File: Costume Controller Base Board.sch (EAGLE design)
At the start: 46 parts, among them J1 USB MICRO, U1 ATMEGA32U4-XUMU, U4 MPU-6050-1, U5 TPS61200, Y1 16MHz KX-7

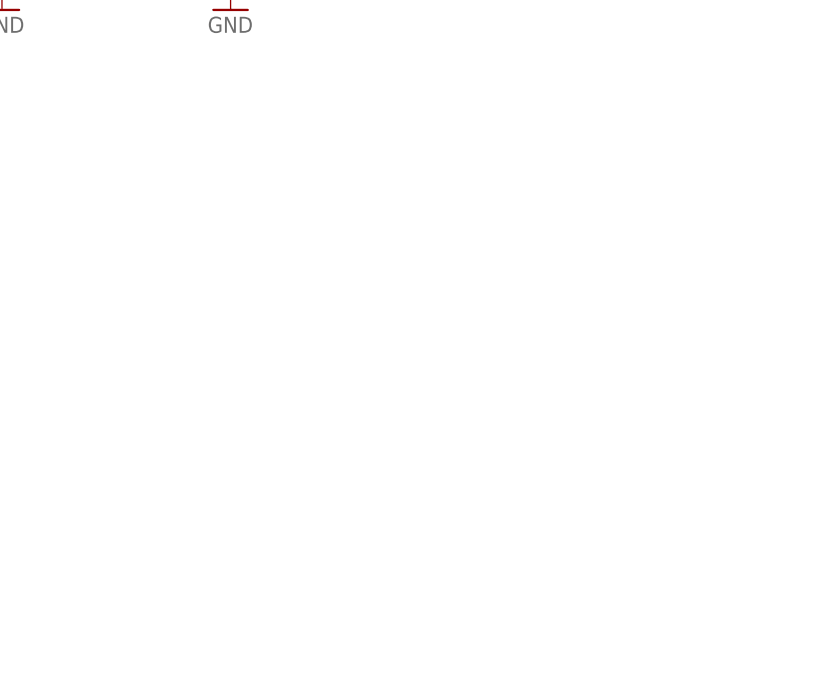
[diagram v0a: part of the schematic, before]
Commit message: Added 3.3v regulator
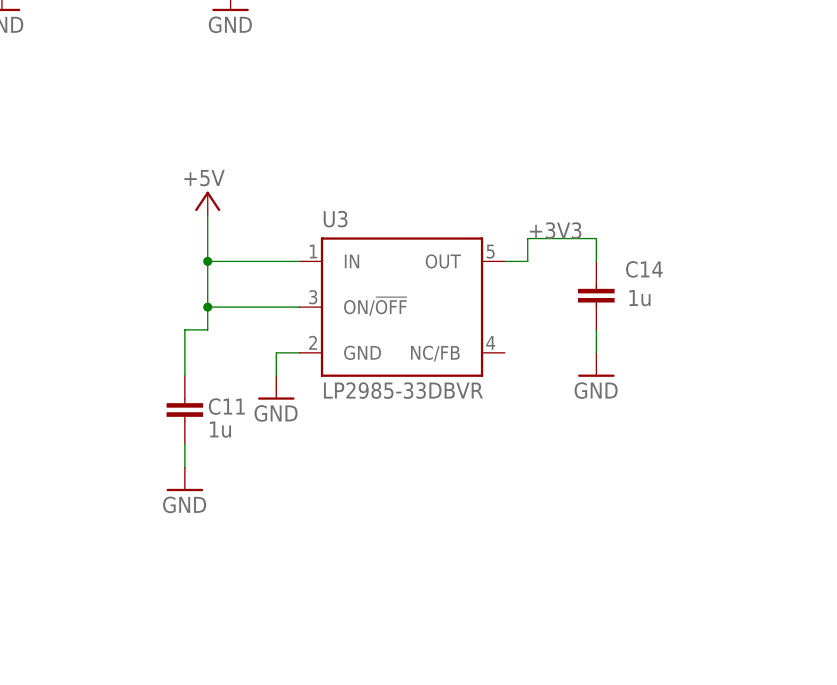
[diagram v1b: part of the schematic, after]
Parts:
- added C11, C14: 1u, SmartPrj:C-EUC0603
- added U3: LP2985-33DBVR, SmartPrj:LP2985-XXDBVR33
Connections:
- new net +3V3: C14.2, U3.OUT
- net +5V: now also C11.2, U3.IN, U3.ON/!OFF
- net GND: now also C11.1, C14.1, U3.GND
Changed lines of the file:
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@@
 <part name="L3" library="SparkFun" deviceset="INDUCTOR" device="." value="4.7uH, 1.2A"/>
 <part name="U$1" library="MyPOW" deviceset="+5V" device=""/>
+<part name="C11" library="SmartPrj" deviceset="C-EU" device="C0603" value="1u"/>
+<part name="GND7" library="supply1" deviceset="GND" device=""/>
+<part name="C14" library="SmartPrj" deviceset="C-EU" device="C0603" value="1u"/>
+<part name="P+10" library="supply1" deviceset="+5V" device=""/>
+<part name="GND21" library="supply1" deviceset="GND" device=""/>
+<part name="U3" library="SmartPrj" deviceset="LP2985-XXDBVR" device="" technology="33" value="LP2985-33DBVR"/>
+<part name="GND13" library="supply1" deviceset="GND" device=""/>
 </parts>
 <sheets>
@@
 </instance>
 <instance part="U$1" gate="G$1" x="-1084.58" y="325.12"/>
+<instance part="C11" gate="G$1" x="-1094.74" y="152.4" smashed="yes" rot="MR180">
+<attribute name="NAME" x="-1092.2" y="154.94" size="1.778" layer="95" rot="MR180"/>
+<attribute name="VALUE" x="-1092.2" y="152.4" size="1.778" layer="96" rot="MR180"/>
+</instance>
+<instance part="GND7" gate="1" x="-1094.74" y="144.78"/>
+<instance part="C14" gate="G$1" x="-1049.02" y="165.1" smashed="yes" rot="R180">
+<attribute name="NAME" x="-1045.845" y="168.402" size="1.778" layer="95"/>
+<attribute name="VALUE" x="-1045.591" y="165.227" size="1.778" layer="96"/>
+</instance>
+<instance part="P+10" gate="1" x="-1092.2" y="177.8" smashed="yes">
+<attribute name="VALUE" x="-1090.295" y="180.34" size="1.778" layer="96" rot="R180"/>
+</instance>
+<instance part="GND21" gate="1" x="-1049.02" y="157.48"/>
+<instance part="U3" gate="G$1" x="-1071.88" y="165.1" smashed="yes">
+<attribute name="NAME" x="-1079.5" y="173.99" size="1.778" layer="95" font="vector"/>
+<attribute name="VALUE" x="-1079.5" y="154.94" size="1.778" layer="96" font="vector"/>
+</instance>
+<instance part="GND13" gate="1" x="-1084.58" y="154.94"/>
 </instances>
 <busses>
@@
 <junction x="-1092.2" y="320.04"/>
 <pinref part="U$1" gate="G$1" pin="+5V"/>
+</segment>
+<segment>
+<wire x1="-1082.04" y1="165.1" x2="-1092.2" y2="165.1" width="0.1524" layer="91"/>
+<wire x1="-1092.2" y1="165.1" x2="-1092.2" y2="170.18" width="0.1524" layer="91"/>
+<wire x1="-1092.2" y1="170.18" x2="-1092.2" y2="175.26" width="0.1524" layer="91"/>
+<wire x1="-1082.04" y1="170.18" x2="-1092.2" y2="170.18" width="0.1524" layer="91"/>
+<wire x1="-1094.74" y1="162.56" x2="-1092.2" y2="162.56" width="0.1524" layer="91"/>
+<wire x1="-1092.2" y1="162.56" x2="-1092.2" y2="165.1" width="0.1524" layer="91"/>
+<wire x1="-1094.74" y1="157.48" x2="-1094.74" y2="162.56" width="0.1524" layer="91"/>
+<junction x="-1092.2" y="170.18"/>
+<junction x="-1092.2" y="165.1"/>
+<pinref part="P+10" gate="1" pin="+5V"/>
+<pinref part="U3" gate="G$1" pin="ON/!OFF"/>
+<pinref part="U3" gate="G$1" pin="IN"/>
+<pinref part="C11" gate="G$1" pin="2"/>
 </segment>
 </net>
@@
 <junction x="-1125.22" y="289.56"/>
 </segment>
+<segment>
+<wire x1="-1094.74" y1="149.86" x2="-1094.74" y2="147.32" width="0.1524" layer="91"/>
+<pinref part="C11" gate="G$1" pin="1"/>
+<pinref part="GND7" gate="1" pin="GND"/>
+</segment>
+<segment>
+<wire x1="-1049.02" y1="160.02" x2="-1049.02" y2="162.56" width="0.1524" layer="91"/>
+<pinref part="C14" gate="G$1" pin="1"/>
+<pinref part="GND21" gate="1" pin="GND"/>
+</segment>
+<segment>
+<wire x1="-1082.04" y1="160.02" x2="-1084.58" y2="160.02" width="0.1524" layer="91"/>
+<wire x1="-1084.58" y1="160.02" x2="-1084.58" y2="157.48" width="0.1524" layer="91"/>
+<pinref part="U3" gate="G$1" pin="GND"/>
+<pinref part="GND13" gate="1" pin="GND"/>
+</segment>
 </net>
 <net name="AREF" class="4">
@@
 </segment>
 </net>
+<net name="+3V3" class="0">
+<segment>
+<wire x1="-1049.02" y1="172.72" x2="-1049.02" y2="170.18" width="0.1524" layer="91"/>
+<wire x1="-1056.64" y1="172.72" x2="-1049.02" y2="172.72" width="0.1524" layer="91"/>
+<wire x1="-1059.18" y1="170.18" x2="-1056.64" y2="170.18" width="0.1524" layer="91"/>
+<wire x1="-1056.64" y1="170.18" x2="-1056.64" y2="172.72" width="0.1524" layer="91"/>
+<label x="-1056.64" y="172.72" size="1.778" layer="95"/>
+<pinref part="C14" gate="G$1" pin="2"/>
+<pinref part="U3" gate="G$1" pin="OUT"/>
+</segment>
+</net>

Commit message: Some joining of grounds and such, need to review nets and busses, eliminated stray resistors, will replace resistor nets with discrete resistors -- www
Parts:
- removed JP6: M10", SparkFun:M10"
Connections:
- removed net N$11: J1.SH1, J1.SH2, J1.SH3, J1.SH4, J1.SH5, J1.SH6, L2.2
- net AUX_SCL: no longer JP6.2
- net AUX_SDA: no longer JP6.1
- net CLKIN: no longer JP6.3
- net FSYNC: no longer JP6.7
- net GND: now also J1.SH1, J1.SH2, J1.SH3, J1.SH4, J1.SH5, J1.SH6, L2.2; no longer JP6.9
- net INT: no longer JP6.8
- net SCL: no longer JP6.6
- net SDA: no longer JP6.5
- net VCC: no longer JP6.10
- net VIO: no longer JP6.4
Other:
- note removed: "1. 3.3v I/O for MPU, or run MCU at 3.3v."
- note removed: "NOT USED"

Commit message: modified nets, removed extraneous components
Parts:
- removed C1, C2, C6: 100n, SmartPrj:C-EUC0603
- removed C5: 1uF, SmartPrj:C-EUC0603
- removed D2: CD1206-S01575, diode:DIODE-MINIMELF
- removed F1: MF-MSMF050-2 500mA, rcl:L-EUL1812
- removed L1, L2: MH2029-300Y, wuerth-elektronik:WE-CBF_0805
- removed RN1: 10K, resistor-dil:4R-NCAY16
- removed RN3: 22R, resistor-dil:4R-NCAY16
- removed SJ1: (no value), SparkFun:SOLDERJUMPER_2WAYPASTE2&3
- removed SJ2, SJ3: SOLDERJUMPERTRACE, SparkFun:SOLDERJUMPERTRACE
- removed Z1, Z2: CG0603MLC-05E, varistor:VARISTORCN0603
- C19: device CH_passive:CAP0805 -> resistor:C-EUC0603
- R2, R3: value NM -> 22; device SmartPrj:R-EU_R0402 -> resistor:R-EU_R0603
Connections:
- removed net A0: U1.(ADC7/TDI)PF7
- removed net A1: U1.(ADC6/TDO)PF6
- removed net A2: U1.(ADC5/TMS)PF5
- removed net A3: U1.(ADC4/TCK)PF4
- removed net A4: U1.(ADC1)PF1
- removed net A5: U1.(ADC0)PF0
- removed net ADO: SJ1.2, U4.AD0
- removed net AGND: C6.1, R2.1, U1.GND3
- removed net AREF: C6.2, U1.AREF
- removed net AVCC: C5.1, L1.2, U1.AVCC, U1.AVCC1
- removed net CLKIN: SJ2.2, U4.CLKIN
- removed net D0/RX: U1.(RXD1/AIN1/INT2)PD2
- removed net D1/TX: U1.(TXD1/INT3)PD3
- removed net D2/SDA: U1.(SDA/INT1)PD1
- removed net D3/SCL: U1.(OC0B/SCL/INT0)PD0
- removed net D4: U1.(ICP1/ADC8)PD4
- removed net D5*: U1.(OC3A/#0C4A)PC6
- removed net D6*: U1.(T0/OC4D/ADC10)PD7
- removed net D7: U1.(INT6/AIN0)PE6
- removed net FSYNC: SJ3.2, U4.FSYNC
- removed net HWB: U1.(#HWB)PE2
- removed net IO10*: U1.(PCINT6/OC1B/OC4B/ADC13)PB6
- removed net IO11*: U1.(PCINT7/OC0A/OC1C/#RTS)PB7
- removed net IO12: U1.(T1/#OC4D/ADC9)PD6
- removed net IO13*: U1.(ICP3/CLK0/OC4A)PC7
- removed net IO8: U1.(ADC11/PCINT4)PB4
- removed net IO9*: U1.(PCINT5/OC1A/#OC4B/ADC12)PB5
- removed net RESET: D2.A, ICSP.5, RN1D.1, U1.RESET
- removed net RXLED: U1.(SS/PCINT0)PB0
- removed net TXLED: U1.(XCK1/#CTS)PD5
- removed net VCC: C17.1, R4.2, R5.2, SJ1.1, U4.VDD
- removed net XUSB: F1.2, J1.VBUS
- net +3V3: now also C17.1, R4.2, R5.2, U4.VDD
- net +5V: now also ICSP.5, U1.AVCC, U1.AVCC1; no longer C1.1, C2.1, D2.C, L1.1, RN1D.2
- net D+: now also R3.1; no longer RN3A.2, Z1.1
- net D-: now also R2.1; no longer RN3D.2, Z2.1
- net GND: now also U4.AD0, U4.CLKIN, U4.FSYNC; no longer C1.2, C2.2, C5.2, L2.2, R2.2, R3.1, SJ1.3, SJ2.1, SJ3.1, Z1.2, Z2.2
- net RD+: now also R3.2; no longer RN3A.1
- net RD-: now also R2.2; no longer RN3D.1
- net SCL: now also U1.(OC0B/SCL/INT0)PD0
- net SDA: now also U1.(SDA/INT1)PD1
- net UGND: no longer L2.1, R3.2
- net VUSB: now also J1.VBUS; no longer F1.1
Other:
- note added: "1. Level shift for MPU logic"
- note removed: "*"
- note removed: "**"
- note removed: "***"
- note removed: "I2C Address Selection*"
- moved on the sheet: C19, R2, R3

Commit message: added TI level translator
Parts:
- added C1: 0.1uF, SparkFun:CAP0603-CAP
- added U2: PCA9306DCUT, Texas Instruments_By_element14_Batch_1:PCA9306DCUT
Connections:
- removed net SCL: R4.1, U1.(OC0B/SCL/INT0)PD0, U4.SCL
- removed net SDA: R5.1, U1.(SDA/INT1)PD1, U4.SDA
- new net SCL2: U1.(OC0B/SCL/INT0)PD0
- new net SDA1: U4.SDA
- new net SDA2: U1.(SDA/INT1)PD1
- net +3V3: now also C1.1
- net GND: now also C1.2
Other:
- note added: "Level-shifter"
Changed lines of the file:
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@@
 <part name="R2" library="resistor" deviceset="R-EU_" device="R0603" value="22"/>
 <part name="R3" library="resistor" deviceset="R-EU_" device="R0603" value="22"/>
+<part name="U2" library="Texas Instruments_By_element14_Batch_1" deviceset="PCA9306DCUT" device=""/>
+<part name="C1" library="SparkFun" deviceset="CAP" device="0603-CAP" value="0.1uF"/>
+<part name="GND2" library="SparkFun" deviceset="GND" device=""/>
+<part name="+3V2" library="supply1" deviceset="+3V3" device=""/>
 </parts>
 <sheets>
@@
 <text x="-1231.9" y="172.72" size="1.778" layer="97">To-Do</text>
 <text x="-1231.9" y="167.64" size="1.778" layer="97">1. Level shift for MPU logic</text>
+<text x="-1013.46" y="256.54" size="1.778" layer="97">Level-shifter</text>
 </plain>
 <instances>
@@
 <instance part="R2" gate="G$1" x="-883.92" y="182.88"/>
 <instance part="R3" gate="G$1" x="-876.3" y="177.8"/>
+<instance part="U2" gate="A" x="-1021.08" y="243.84"/>
+<instance part="C1" gate="G$1" x="-1069.34" y="259.08"/>
+<instance part="GND2" gate="1" x="-1069.34" y="246.38"/>
+<instance part="+3V2" gate="G$1" x="-1069.34" y="271.78"/>
 </instances>
 <busses>
@@
 <pinref part="GND6" gate="1" pin="GND"/>
 </segment>
+<segment>
+<pinref part="GND2" gate="1" pin="GND"/>
+<pinref part="C1" gate="G$1" pin="2"/>
+<wire x1="-1069.34" y1="248.92" x2="-1069.34" y2="256.54" width="0.1524" layer="91"/>
+</segment>
 </net>
 <net name="VIN" class="1">
@@
 </segment>
 </net>
-<net name="SCL" class="0">
-<segment>
-<wire x1="-1104.9" y1="231.14" x2="-1104.9" y2="220.98" width="0.1524" layer="91"/>
-<wire x1="-1104.9" y1="220.98" x2="-1125.22" y2="220.98" width="0.1524" layer="91"/>
-<label x="-1122.68" y="220.98" size="1.778" layer="95"/>
-<pinref part="R4" gate="G$1" pin="1"/>
-<pinref part="U4" gate="G$1" pin="SCL"/>
-</segment>
+<net name="SCL2" class="0">
 <segment>
 <wire x1="-741.68" y1="251.46" x2="-769.62" y2="251.46" width="0.1524" layer="91"/>
 <label x="-759.46" y="251.46" size="1.778" layer="95"/>
 <pinref part="U1" gate="G$1" pin="(OC0B/SCL/INT0)PD0"/>
-</segment>
-</net>
-<net name="SDA" class="0">
-<segment>
-<wire x1="-1097.28" y1="231.14" x2="-1097.28" y2="218.44" width="0.1524" layer="91"/>
-<wire x1="-1097.28" y1="218.44" x2="-1125.22" y2="218.44" width="0.1524" layer="91"/>
-<label x="-1122.68" y="218.44" size="1.778" layer="95"/>
-<pinref part="R5" gate="G$1" pin="1"/>
-<pinref part="U4" gate="G$1" pin="SDA"/>
-</segment>
-<segment>
-<wire x1="-741.68" y1="254" x2="-769.62" y2="254" width="0.1524" layer="91"/>
+<wire x1="-741.68" y1="251.46" x2="-741.68" y2="213.36" width="0.1524" layer="91"/>
+<wire x1="-741.68" y1="213.36" x2="-980.44" y2="213.36" width="0.1524" layer="91"/>
+<wire x1="-980.44" y1="213.36" x2="-980.44" y2="238.76" width="0.1524" layer="91"/>
+<wire x1="-980.44" y1="238.76" x2="-1005.84" y2="238.76" width="0.1524" layer="91"/>
+</segment>
+</net>
+<net name="SDA2" class="0">
+<segment>
+<wire x1="-734.06" y1="254" x2="-769.62" y2="254" width="0.1524" layer="91"/>
 <label x="-759.46" y="254" size="1.778" layer="95"/>
 <pinref part="U1" gate="G$1" pin="(SDA/INT1)PD1"/>
+<wire x1="-734.06" y1="254" x2="-734.06" y2="210.82" width="0.1524" layer="91"/>
+<wire x1="-734.06" y1="210.82" x2="-982.98" y2="210.82" width="0.1524" layer="91"/>
+<wire x1="-982.98" y1="210.82" x2="-982.98" y2="236.22" width="0.1524" layer="91"/>
+<wire x1="-982.98" y1="236.22" x2="-1005.84" y2="236.22" width="0.1524" layer="91"/>
 </segment>
 </net>
@@
 <wire x1="-1097.28" y1="256.54" x2="-1097.28" y2="241.3" width="0.1524" layer="91"/>
 </segment>
-</net>
+<segment>
+<pinref part="C1" gate="G$1" pin="1"/>
+<wire x1="-1069.34" y1="264.16" x2="-1069.34" y2="266.7" width="0.1524" layer="91"/>
+<pinref part="+3V2" gate="G$1" pin="+3V3"/>
+<wire x1="-1069.34" y1="266.7" x2="-1069.34" y2="269.24" width="0.1524" layer="91"/>
+<wire x1="-1069.34" y1="266.7" x2="-1041.4" y2="266.7" width="0.1524" layer="91"/>
+<wire x1="-1041.4" y1="266.7" x2="-1041.4" y2="246.38" width="0.1524" layer="91"/>
+<wire x1="-1041.4" y1="246.38" x2="-1036.32" y2="246.38" width="0.1524" layer="91"/>
+</segment>
+</net>
+<net name="SCL1" class="0">
+<segment>
+<wire x1="-1127.76" y1="220.98" x2="-993.14" y2="220.98" width="0.1524" layer="91"/>
+<wire x1="-993.14" y1="220.98" x2="-993.14" y2="246.38" width="0.1524" layer="91"/>
+<wire x1="-993.14" y1="246.38" x2="-1005.84" y2="246.38" width="0.1524" layer="91"/>
+</segment>
+</net>
+<net name="SDA1" class="0">
+<segment>
+<pinref part="U4" gate="G$1" pin="SDA"/>
+<wire x1="-1125.22" y1="218.44" x2="-995.68" y2="218.44" width="0.1524" layer="91"/>
+<wire x1="-995.68" y1="218.44" x2="-995.68" y2="243.84" width="0.1524" layer="91"/>
+<wire x1="-995.68" y1="243.84" x2="-1005.84" y2="243.84" width="0.1524" layer="91"/>
+</segment>
+</net>

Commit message: complete schematic, though VUSB needs further study, probably won't power +5v
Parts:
- added C2: 0.1uF, SparkFun:CAP0603-CAP
- added R8: 10k, SparkFun:RESISTOR0603-RES
- added X1: 09FLZ-SM1, con-jst:09FLZ-SM1
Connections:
- new net N$15: U1.(SS/PCINT0)PB0
- new net N$2: C2.1, R8.1
- new net STRAND1: U1.(RXD1/AIN1/INT2)PD2, X1-1.1
- new net STRAND2: U1.(TXD1/INT3)PD3
- new net STRAND3: U1.(ICP1/ADC8)PD4
- new net STRAND4: U1.(XCK1/#CTS)PD5, X1-4.1
- new net STRAND5: U1.(T1/#OC4D/ADC9)PD6, X1-5.1
- new net STRAND6: U1.(T0/OC4D/ADC10)PD7, X1-6.1
- new net STRAND7: U1.(#HWB)PE2, X1-7.1
- new net STRAND8: U1.(OC3A/#0C4A)PC6
- new net STRAND9: U1.(ICP3/CLK0/OC4A)PC7, X1-9.1
- net +5V: now also R8.2
- net GND: now also C2.2
- net INT: now also U1.(INT6/AIN0)PE6
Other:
- note added: "ENABLE tied high, could be IO"
- note added: "JST Connector 9 pin"
